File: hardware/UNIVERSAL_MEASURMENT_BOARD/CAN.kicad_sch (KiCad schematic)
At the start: 17 parts, among them U18 ADM3057EBRWZ

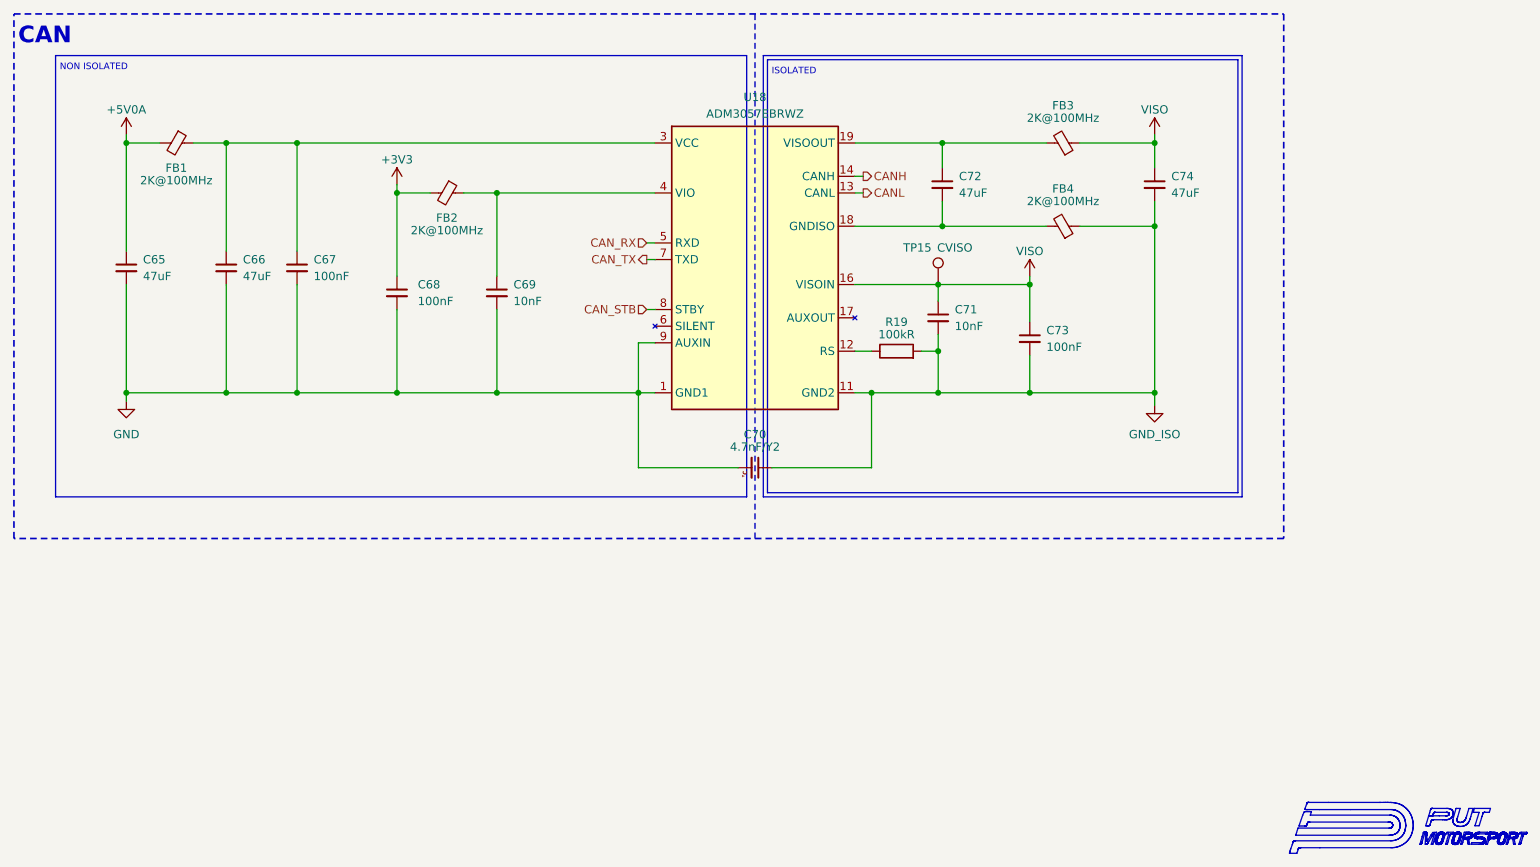
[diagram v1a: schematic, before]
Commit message: Reduced PCB dimensions, working on power section
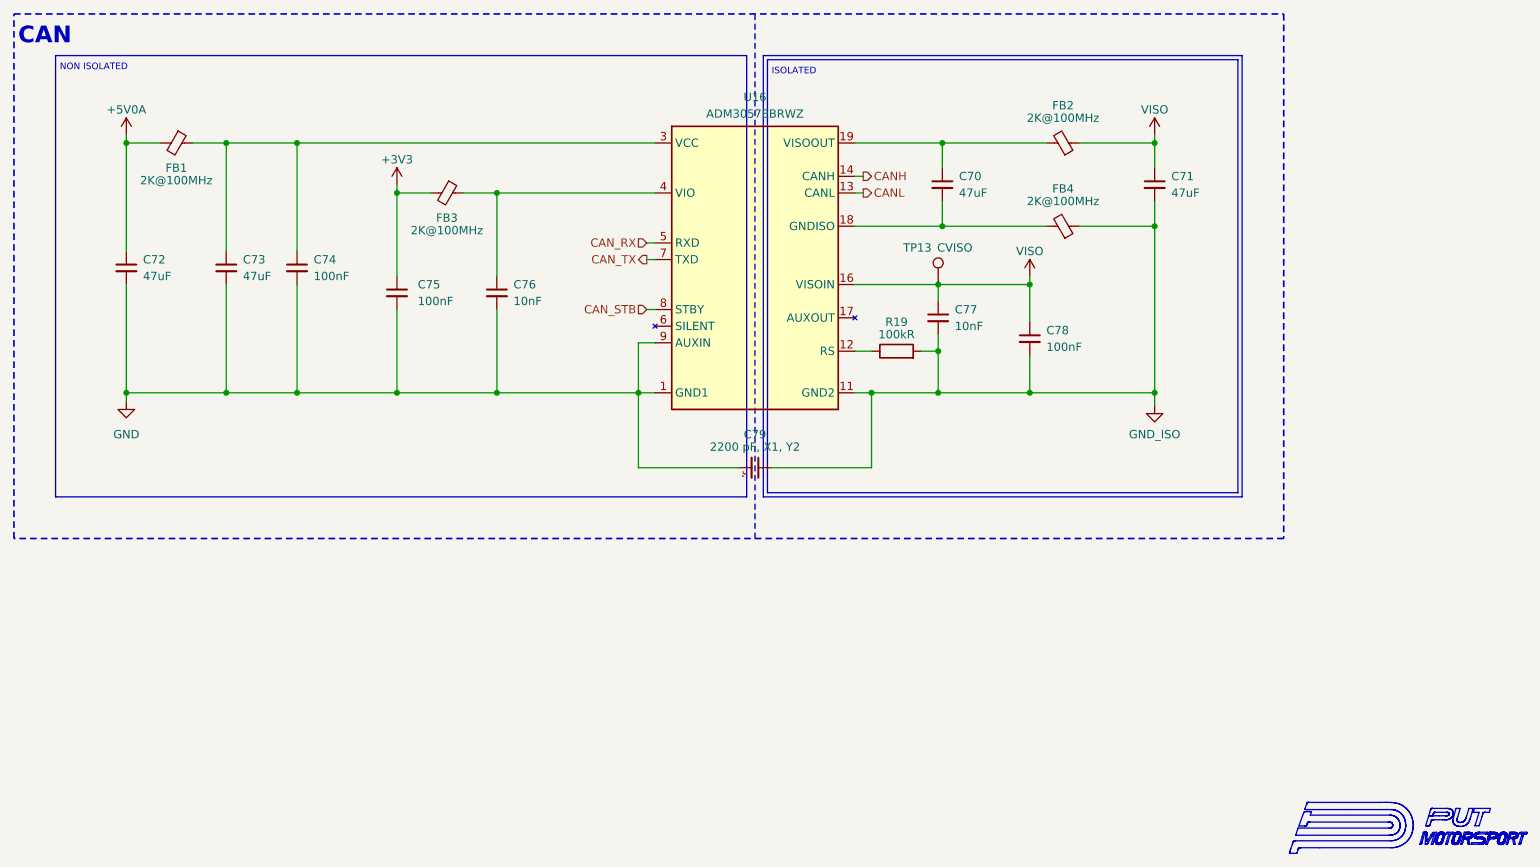
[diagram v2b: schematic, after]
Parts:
- C79: renamed from C70; value 4.7nF/Y2 -> 2200 pF, X1, Y2
- renumbered C72 to C70, C74 to C71, C65 to C72, C66 to C73, C67 to C74, C68 to C75, C69 to C76, C71 to C77, C73 to C78, FB3 to FB2, FB2 to FB3, TP15 to TP13, U18 to U16
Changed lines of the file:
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@@
 		(dnp no)
 		(fields_autoplaced yes)
-		(property "Reference" "C67"
+		(property "Reference" "C74"
 			(at 97.155 87.0012 0)
 			(show_name no)
@@
 			(project "UNIVERSAL_MEASURMENT_BOARD"
 				(path "/92c00310-4384-4ef3-9368-efad75526047/007c1dd5-a7d9-42e3-b7c2-f5a2b9d94f0b"
-					(reference "C67")
+					(reference "C74")
 					(unit 1)
 				)
@@
 		(in_pos_files yes)
 		(dnp no)
-		(property "Reference" "C70"
+		(property "Reference" "C79"
 			(at 164.465 113.665 0)
 			(show_name no)
@@
 			)
 		)
-		(property "Value" "4.7nF/Y2"
+		(property "Value" "2200 pF, X1, Y2"
 			(at 164.465 115.57 0)
 			(show_name no)
@@
 			(project "UNIVERSAL_MEASURMENT_BOARD"
 				(path "/92c00310-4384-4ef3-9368-efad75526047/007c1dd5-a7d9-42e3-b7c2-f5a2b9d94f0b"
-					(reference "C70")
+					(reference "C79")
 					(unit 1)
 				)
@@
 		(in_pos_files yes)
 		(dnp no)
-		(property "Reference" "C72"
+		(property "Reference" "C70"
 			(at 195.58 74.295 0)
 			(show_name no)
@@
 			(project "UNIVERSAL_MEASURMENT_BOARD"
 				(path "/92c00310-4384-4ef3-9368-efad75526047/007c1dd5-a7d9-42e3-b7c2-f5a2b9d94f0b"
-					(reference "C72")
+					(reference "C70")
 					(unit 1)
 				)
@@
 		(in_pos_files yes)
 		(dnp no)
-		(property "Reference" "C74"
+		(property "Reference" "C71"
 			(at 227.965 74.3012 0)
 			(show_name no)
@@
 			(project "UNIVERSAL_MEASURMENT_BOARD"
 				(path "/92c00310-4384-4ef3-9368-efad75526047/007c1dd5-a7d9-42e3-b7c2-f5a2b9d94f0b"
-					(reference "C74")
+					(reference "C71")
 					(unit 1)
 				)
@@
 		(dnp no)
 		(fields_autoplaced yes)
-		(property "Reference" "C71"
+		(property "Reference" "C77"
 			(at 194.945 94.6212 0)
 			(show_name no)
@@
 			(project "UNIVERSAL_MEASURMENT_BOARD"
 				(path "/92c00310-4384-4ef3-9368-efad75526047/007c1dd5-a7d9-42e3-b7c2-f5a2b9d94f0b"
-					(reference "C71")
+					(reference "C77")
 					(unit 1)
 				)
@@
 		(dnp no)
 		(fields_autoplaced yes)
-		(property "Reference" "#PWR0150"
+		(property "Reference" "#PWR0159"
 			(at 225.425 115.57 0)
 			(hide yes)
@@
 			(project "UNIVERSAL_MEASURMENT_BOARD"
 				(path "/92c00310-4384-4ef3-9368-efad75526047/007c1dd5-a7d9-42e3-b7c2-f5a2b9d94f0b"
-					(reference "#PWR0150")
+					(reference "#PWR0159")
 					(unit 1)
 				)
@@
 		(dnp no)
 		(fields_autoplaced yes)
-		(property "Reference" "#PWR0145"
+		(property "Reference" "#PWR0158"
 			(at 68.58 114.935 0)
 			(hide yes)
@@
 			(project "UNIVERSAL_MEASURMENT_BOARD"
 				(path "/92c00310-4384-4ef3-9368-efad75526047/007c1dd5-a7d9-42e3-b7c2-f5a2b9d94f0b"
-					(reference "#PWR0145")
+					(reference "#PWR0158")
 					(unit 1)
 				)
@@
 		(in_pos_files yes)
 		(dnp no)
-		(property "Reference" "#PWR0148"
+		(property "Reference" "#PWR0155"
 			(at 225.425 71.755 0)
 			(hide yes)
@@
 			(project "UNIVERSAL_MEASURMENT_BOARD"
 				(path "/92c00310-4384-4ef3-9368-efad75526047/007c1dd5-a7d9-42e3-b7c2-f5a2b9d94f0b"
-					(reference "#PWR0148")
+					(reference "#PWR0155")
 					(unit 1)
 				)
@@
 		(dnp no)
 		(fields_autoplaced yes)
-		(property "Reference" "C69"
+		(property "Reference" "C76"
 			(at 127.635 90.8112 0)
 			(show_name no)
@@
 			(project "UNIVERSAL_MEASURMENT_BOARD"
 				(path "/92c00310-4384-4ef3-9368-efad75526047/007c1dd5-a7d9-42e3-b7c2-f5a2b9d94f0b"
-					(reference "C69")
+					(reference "C76")
 					(unit 1)
 				)
@@
 		(in_pos_files yes)
 		(dnp no)
-		(property "Reference" "FB2"
+		(property "Reference" "FB3"
 			(at 117.475 80.645 90)
 			(show_name no)
@@
 			(project "UNIVERSAL_MEASURMENT_BOARD"
 				(path "/92c00310-4384-4ef3-9368-efad75526047/007c1dd5-a7d9-42e3-b7c2-f5a2b9d94f0b"
-					(reference "FB2")
+					(reference "FB3")
 					(unit 1)
 				)
@@
 		(dnp no)
 		(fields_autoplaced yes)
-		(property "Reference" "U18"
+		(property "Reference" "U16"
 			(at 164.465 62.23 0)
 			(show_name no)
@@
 			(project "UNIVERSAL_MEASURMENT_BOARD"
 				(path "/92c00310-4384-4ef3-9368-efad75526047/007c1dd5-a7d9-42e3-b7c2-f5a2b9d94f0b"
-					(reference "U18")
+					(reference "U16")
 					(unit 1)
 				)
@@
 		(dnp no)
 		(fields_autoplaced yes)
-		(property "Reference" "C73"
+		(property "Reference" "C78"
 			(at 208.915 97.7962 0)
 			(show_name no)
@@
 			(project "UNIVERSAL_MEASURMENT_BOARD"
 				(path "/92c00310-4384-4ef3-9368-efad75526047/007c1dd5-a7d9-42e3-b7c2-f5a2b9d94f0b"
-					(reference "C73")
+					(reference "C78")
 					(unit 1)
 				)
@@
 		(in_pos_files yes)
 		(dnp no)
-		(property "Reference" "#PWR0147"
+		(property "Reference" "#PWR0157"
 			(at 206.375 93.345 0)
 			(hide yes)
@@
 			(project "UNIVERSAL_MEASURMENT_BOARD"
 				(path "/92c00310-4384-4ef3-9368-efad75526047/007c1dd5-a7d9-42e3-b7c2-f5a2b9d94f0b"
-					(reference "#PWR0147")
+					(reference "#PWR0157")
 					(unit 1)
 				)
@@
 		(dnp no)
 		(fields_autoplaced yes)
-		(property "Reference" "C65"
+		(property "Reference" "C72"
 			(at 71.12 87.0012 0)
 			(show_name no)
@@
 			(project "UNIVERSAL_MEASURMENT_BOARD"
 				(path "/92c00310-4384-4ef3-9368-efad75526047/007c1dd5-a7d9-42e3-b7c2-f5a2b9d94f0b"
-					(reference "C65")
+					(reference "C72")
 					(unit 1)
 				)
@@
 		(in_pos_files yes)
 		(dnp no)
-		(property "Reference" "FB3"
+		(property "Reference" "FB2"
 			(at 211.455 63.5 90)
 			(show_name no)
@@
 			(project "UNIVERSAL_MEASURMENT_BOARD"
 				(path "/92c00310-4384-4ef3-9368-efad75526047/007c1dd5-a7d9-42e3-b7c2-f5a2b9d94f0b"
-					(reference "FB3")
+					(reference "FB2")
 					(unit 1)
 				)
@@
 		(in_pos_files yes)
 		(dnp no)
-		(property "Reference" "TP15"
+		(property "Reference" "TP13"
 			(at 189.23 84.455 0)
 			(show_name no)
@@
 			(project "UNIVERSAL_MEASURMENT_BOARD"
 				(path "/92c00310-4384-4ef3-9368-efad75526047/007c1dd5-a7d9-42e3-b7c2-f5a2b9d94f0b"
-					(reference "TP15")
+					(reference "TP13")
 					(unit 1)
 				)
@@
 		(dnp no)
 		(fields_autoplaced yes)
-		(property "Reference" "C68"
+		(property "Reference" "C75"
 			(at 113.03 90.8112 0)
 			(show_name no)
@@
 			(project "UNIVERSAL_MEASURMENT_BOARD"
 				(path "/92c00310-4384-4ef3-9368-efad75526047/007c1dd5-a7d9-42e3-b7c2-f5a2b9d94f0b"
-					(reference "C68")
+					(reference "C75")
 					(unit 1)
 				)
@@
 		(in_pos_files yes)
 		(dnp no)
-		(property "Reference" "#PWR0146"
+		(property "Reference" "#PWR0156"
 			(at 109.855 79.375 0)
 			(hide yes)
@@
 			(project "UNIVERSAL_MEASURMENT_BOARD"
 				(path "/92c00310-4384-4ef3-9368-efad75526047/007c1dd5-a7d9-42e3-b7c2-f5a2b9d94f0b"
-					(reference "#PWR0146")
+					(reference "#PWR0156")
 					(unit 1)
 				)
@@
 		(in_pos_files yes)
 		(dnp no)
-		(property "Reference" "#PWR0144"
+		(property "Reference" "#PWR0154"
 			(at 68.58 71.755 0)
 			(hide yes)
@@
 			(project "UNIVERSAL_MEASURMENT_BOARD"
 				(path "/92c00310-4384-4ef3-9368-efad75526047/007c1dd5-a7d9-42e3-b7c2-f5a2b9d94f0b"
-					(reference "#PWR0144")
+					(reference "#PWR0154")
 					(unit 1)
 				)
@@
 		(dnp no)
 		(fields_autoplaced yes)
-		(property "Reference" "C66"
+		(property "Reference" "C73"
 			(at 86.36 87.0012 0)
 			(show_name no)
@@
 			(project "UNIVERSAL_MEASURMENT_BOARD"
 				(path "/92c00310-4384-4ef3-9368-efad75526047/007c1dd5-a7d9-42e3-b7c2-f5a2b9d94f0b"
-					(reference "C66")
-					(unit 1)
-				)
+					(reference "C73")
+					(unit 1)
+				)
